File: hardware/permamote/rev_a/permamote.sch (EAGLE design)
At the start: 130 parts, among them J1 TC2030-JLINK-NL, J5 MICRO_USB_B_HIROSE_ZX62R-B-5P, Q1 PMDXB950UPEL, Q10 PMDXB950UPEL, Q2 PMDXB950UPEL, Q3 PMDXB950UPEL, Q4 PMDXB950UPEL, Q5 PMDXB950UPEL, Q6 PMDXB950UPEL, Q7 PMDXB950UPEL, Q8 PMDXB950UPEL, U1 AB1815-T3, U10 NRF52840, U11 SI7021-A20-GM1, U12 FT232RQ, U2 BQ25505, U3 EKMB1101111, U4 ISL29125, U5 LIS2DW12, U6 MAX17222, U7 MAX44009, U8 MS5637-02BA03, X1 32MHz, X3 32.768kHz, X4 ABS07-32.768KHZ-7-T

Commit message: Rename passives
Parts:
- removed C35: 4.7uF, passives:CAPACITOR0402_CAP
- removed C37, C38, C39: 10uF, passives:CAPACITOR0603_CAP
- removed C41: 0.1uF, passives:CAPACITOR0402_CAP
- removed C42, C43: DNP, passives:CAPACITOR0402_CAP
- removed L8: 1uH, passives:INDUCTORIHL
- removed R28: 6.19M, passives:RESISTOR0402_RES
- removed R29: 6.81M, passives:RESISTOR0402_RES
- removed U12: FT232RQ, ftdichip:FT232RQ
- added C14, C15, C16, C19: 0.1uF, passives:CAPACITOR0402_CAP
- added C28: 4.7uF, passives:CAPACITOR0603_CAP
- added C6: 12pF, passives:CAPACITOR0402_CAP
- added C9: 10nF, passives:CAPACITOR0402_CAP
- added L2: 15nH, passives:INDUCTOR0402
- added R19: 7.32M, passives:RESISTOR0402_RES
- added R20: 8.87M, passives:RESISTOR0402_RES
- added U9: MS5637-02BA03, chips:MS5637-02BA03
- C10: value 12pF -> 10nF; DIGIKEY 490-6197-1-ND -> 490-4516-1-ND
- C11: value 12pF -> 47nF; DIGIKEY 490-6197-1-ND -> 445-1264-1-ND
- C12: value 47pF -> 0.1uF; DIGIKEY 490-5942-1-ND -> 490-6328-1-ND
- C13: value 100pF -> 0.1uF; DIGIKEY 490-5922-1-ND -> 490-6328-1-ND
- C17: value 10nF -> 0.1uF; DIGIKEY 490-4516-1-ND -> 490-6328-1-ND
- C18: value 47nF -> 0.1uF; DIGIKEY 445-1264-1-ND -> 490-6328-1-ND
- C21, C22, C23, C24, C25: value 0.1uF -> 1uF; DIGIKEY 490-6328-1-ND -> 490-7195-1-ND
- C26, C27: value 0.1uF -> 4.7uF; DIGIKEY 490-6328-1-ND -> 445-5947-1-ND
- C29, C30, C31: value 1uF -> 10uF; device passives:CAPACITOR0402_CAP -> passives:CAPACITOR0603_CAP; DIGIKEY 490-7195-1-ND -> 490-3896-1-ND
- C3: value 0.01uF -> 12pF; DIGIKEY 490-4516-1-ND -> 490-6197-1-ND
- C32, C33: value 1uF -> DNP; DIGIKEY 490-7195-1-ND -> (none)
- C7: value 4.7uF -> 47pF; DIGIKEY 445-5947-1-ND -> 490-5942-1-ND
- C8: value 4.7uF -> 100pF; device passives:CAPACITOR0603_CAP -> passives:CAPACITOR0402_CAP; DIGIKEY 445-5947-1-ND -> 490-5922-1-ND
- L3: value 15nH -> 1uH; device passives:INDUCTOR0402 -> passives:INDUCTORIHL; DIGIKEY 587-1521-1-ND -> 541-1319-1-ND; MPN (none) -> IHLP1212BZER1R0M11
- R1, R2, R3: value 10kΩ -> 470; DIGIKEY 311-10KJRCT-ND -> 311-470JRCT-ND
- R10: value 6.04k -> 10k; DIGIKEY YAG3306CT-ND -> 311-10KJRCT-ND
- R11: value 3.9M -> 10k; DIGIKEY YAG3306CT-ND -> 311-10KJRCT-ND
- R12: value 8.87M -> 10k; DIGIKEY YAG3306CT-ND -> 311-10KJRCT-ND
- R13: value 4.22M -> 80.6k; device passives:RESISTOR0402_RES -> passives:RESISTOR0603_RES; DIGIKEY YAG3306CT-ND -> 311-80.6KHRCT-ND
- R14: value 7.32M -> 3.9M
- R15: value 9.09M -> 4.22M
- R17: value 470 -> 6.19M; DIGIKEY 311-470JRCT-ND -> YAG3306CT-ND
- R18: value 470 -> 6.81M; DIGIKEY 311-470JRCT-ND -> YAG3306CT-ND
- R21: value 6.04k -> 9.09M
- R22: value 33MΩ -> 33M
- R23, R24, R25, R26, R27: value 100MΩ -> 100M
- R4, R5: value 10kΩ -> 6.04k; DIGIKEY 311-10KJRCT-ND -> YAG3306CT-ND
- R6, R7: value 10kΩ -> 10k
- R8: value 470 -> 10k; DIGIKEY 311-470JRCT-ND -> 311-10KJRCT-ND
- R9: value 80.6kΩ -> 10k; device passives:RESISTOR0603_RES -> passives:RESISTOR0402_RES; DIGIKEY 311-80.6KHRCT-ND -> 311-10KJRCT-ND
- U4: value ISL29125 -> FT232RQ; device chips:ISL29125 -> ftdichip:FT232RQ
- U5: value LIS2DW12 -> ISL29125; device chips:LIS2DW12 -> chips:ISL29125
- U6: value MAX17222 -> LIS2DW12; device chips:MAX17222 -> chips:LIS2DW12
- U7: value MAX44009 -> MAX17222; device chips:MAX44009 -> chips:MAX17222
- U8: value MS5637-02BA03 -> MAX44009; device chips:MS5637-02BA03 -> chips:MAX44009
- renumbered L6 to L4, L7 to L5
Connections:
- net !CLR_INT: now also R8.1, U5.!INT; no longer R4.1, U4.!INT
- net !FTDI_RESET: now also U4.!RESET; no longer U12.!RESET
- net !LT_INT: now also R9.1, U8.!INT; no longer R5.1, U7.!INT
- net !RST: now also R11.1; no longer R7.1
- net !RTC_EXTR: now also R10.1; no longer R6.1
- net ACC_CS: now also U6.CS; no longer U5.CS
- net ACC_INT1: now also U6.INT1; no longer U5.INT1
- net ACC_INT2: now also U6.INT2; no longer U5.INT2
- net D+: now also U4.USBDP; no longer U12.USBDP
- net D-: now also U4.USBDM; no longer U12.USBDM
- net FTDI_VCCIO: now also U4.VCCIO; no longer U12.VCCIO
- net GND: now also C10.2, C11.2, C14.2, C15.2, C16.2, C19.2, C28.2, C3.1, C6.1, C9.2, R18.1, R21.1, U4.GND@1, U4.GND@2, U4.GND@A, U4.TEST, U8.A0, U9.GND; no longer C10.1, C11.1, C3.2, C35.2, C37.2, C38.2, C39.2, C41.2, C42.2, C43.2, R29.1, R9.1, U12.GND, U12.GND@1, U12.GND@2, U12.GND@A, U12.TEST, U7.A0
- net LED_BLUE: now also R3.2; no longer R18.2
- net LED_GREEN: now also R2.2; no longer R17.2
- net LED_RED: now also R1.2; no longer R8.2
- net MISO: now also U6.MISO/SA0; no longer U5.MISO/SA0
- net MOSI: now also U6.MOSI/SDA; no longer U5.MOSI/SDA
- net N$1: now also R14.2, R4.2; no longer R11.2, R21.2
- net N$12: now also R13.2, U7.SEL; no longer R9.2, U6.SEL
- net N$13: now also C20.1, U4.3V3OUT; no longer C41.1, U12.3V3OUT
- net N$14: now also U7.EN; no longer U6.EN
- net N$15: now also R1.1; no longer R8.1
- net N$16: now also R19.2, R5.2; no longer R10.2, R14.2
- net N$17: now also R2.1; no longer R17.1
- net N$18: now also R19.1, R21.2; no longer R11.1, R15.2
- net N$19: now also R3.1; no longer R18.1
- net N$2: now also C14.1; no longer C22.1
- net N$20: now also U8.VCC; no longer U7.VCC
- net N$21: now also U9.VDD; no longer U8.VDD
- net N$25: now also C7.1; no longer C12.1
- net N$26: now also C32.1; no longer C42.1
- net N$27: now also C33.1; no longer C43.1
- net N$3: now also C11.1, C22.1, L2.1; no longer C18.1, C30.1, L3.1
- net N$31: now also U5.VDD; no longer U4.VDD
- net N$34: now also U9.SCL; no longer U8.SCL
- net N$4: now also C8.1; no longer C13.1
- net N$41: now also U9.SDA; no longer U8.SDA
- net N$49: now also L2.2; no longer L3.2
- net N$51: now also U8.SDA; no longer U7.SDA
- net N$52: now also U8.SCL; no longer U7.SCL
- net N$54: now also U5.SDA; no longer U4.SDA
- net N$55: now also U5.SCL; no longer U4.SCL
- net N$57: now also R15.2, R17.1, R18.2, R20.1; no longer R12.1, R13.2, R28.1, R29.2
- net N$58: now also R17.2, R20.2, R4.1, R5.1; no longer R10.1, R12.2, R21.1, R28.2
- net N$8: now also C3.2; no longer C4.2
- net N$9: now also C4.2; no longer C5.2
- net RXD: now also U4.RXD; no longer U12.RXD
- net SCK: now also U6.SCL/SPC; no longer U5.SCL/SPC
- net SCL: now also R6.1; no longer R2.1
- net SDA: now also R7.1; no longer R3.1
- net SW: now also L3.2, U7.LX; no longer L8.2, U6.LX
- net TXD: now also U4.TXD; no longer U12.TXD
- net USB_5V: now also U4.VCC; no longer U12.VCC
- net VCC: now also C12.1, C13.1, C15.1, C16.1, C17.1, C18.1, C19.1, C30.1, R10.2, R11.2, R12.2, R8.2, R9.2, U6.VCC, U6.VDD_IO, U7.OUT; no longer C20.1, C27.1, C29.1, C32.1, C33.1, C35.1, C38.1, C39.1, R1.2, R2.2, R3.2, R4.2, R5.2, U5.VCC, U5.VDD_IO, U6.OUT
- net VOC_SAMP_VSTOR: now also C10.1, C27.1; no longer C3.1, C7.1
- net VREF_SAMP: now also C9.1; no longer C17.1
- net VSOL: now also C28.1; no longer C8.1
- net VSW: now also C29.1, L3.1, U7.IN; no longer C37.1, L8.1, U6.IN
- net WDI: now also R12.1; no longer R1.1
- net XL1: now also C6.2; no longer C11.2
- net XL2: now also C5.2; no longer C10.2
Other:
- moved on the sheet: C11, C12, C13, C21, C22, C24, C31, C33, C4, C5, R13, R14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

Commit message: update parts
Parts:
- C28: device passives:CAPACITOR0603_CAP -> passives:CAPACITOR0402_CAP
- J5: value MICRO_USB_B_HIROSE_ZX62R-B-5P -> MICRO_USB_B_HIROSE_ZX62R-B-5P(30); device connector:MICRO_USB_B_HIROSE_ZX62R-B-5P -> connector:MICRO_USB_B_HIROSE_ZX62R-B-5P(30)
- R14: DIGIKEY YAG3306CT-ND -> YAG3301CT-ND; MPN (none) -> RC0402JR-073M9L
- R15: value 4.22M -> DNP
- R16: value 5.62M -> DNP
- R17: value 6.19M -> 6.2M; DIGIKEY YAG3306CT-ND -> YAG3309CT-ND; MPN (none) -> RC0402JR-076M2L
- R18: value 6.81M -> 6.8M; DIGIKEY YAG3306CT-ND -> YAG3310CT-ND; MPN (none) -> RC0402JR-076M8L
- R19: value 7.32M -> DNP
- R20: value 8.87M -> DNP
- R21: value 9.09M -> 9.1M; DIGIKEY YAG3306CT-ND -> YAG3322CT-ND; MPN (none) -> RC0402JR-079M1L
- R4: DIGIKEY YAG3306CT-ND -> YAG2293CT-ND; MPN (none) -> RC0402FR-076K04L
- R5: value 6.04k -> DNP
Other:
- note added: "Divider for Other"
- note removed: "Divider for Lithium Polymer"
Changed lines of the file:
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@@
 <part name="Q6" library="fets" deviceset="PMDXB950UPEL" device=""/>
 <part name="R14" library="passives" deviceset="RESISTOR" device="0402_RES" value="3.9M">
-<attribute name="DIGIKEY" value="YAG3306CT-ND"/>
-</part>
-<part name="R21" library="passives" deviceset="RESISTOR" device="0402_RES" value="9.09M">
-<attribute name="DIGIKEY" value="YAG3306CT-ND"/>
+<attribute name="DIGIKEY" value="YAG3301CT-ND"/>
+<attribute name="MPN" value="RC0402JR-073M9L"/>
+</part>
+<part name="R21" library="passives" deviceset="RESISTOR" device="0402_RES" value="9.1M">
+<attribute name="DIGIKEY" value="YAG3322CT-ND"/>
+<attribute name="MPN" value="RC0402JR-079M1L"/>
 </part>
 <part name="GND21" library="supply1" library_urn="urn:adsk.eagle:library:371" deviceset="GND" device=""/>
 <part name="R4" library="passives" deviceset="RESISTOR" device="0402_RES" value="6.04k">
-<attribute name="DIGIKEY" value="YAG3306CT-ND"/>
-</part>
-<part name="R17" library="passives" deviceset="RESISTOR" device="0402_RES" value="6.19M">
-<attribute name="DIGIKEY" value="YAG3306CT-ND"/>
-</part>
-<part name="R18" library="passives" deviceset="RESISTOR" device="0402_RES" value="6.81M">
-<attribute name="DIGIKEY" value="YAG3306CT-ND"/>
+<attribute name="DIGIKEY" value="YAG2293CT-ND"/>
+<attribute name="MPN" value="RC0402FR-076K04L"/>
+</part>
+<part name="R17" library="passives" deviceset="RESISTOR" device="0402_RES" value="6.2M">
+<attribute name="DIGIKEY" value="YAG3309CT-ND"/>
+<attribute name="MPN" value="RC0402JR-076M2L"/>
+</part>
+<part name="R18" library="passives" deviceset="RESISTOR" device="0402_RES" value="6.8M">
+<attribute name="DIGIKEY" value="YAG3310CT-ND"/>
+<attribute name="MPN" value="RC0402JR-076M8L"/>
 </part>
 <part name="GND22" library="supply1" library_urn="urn:adsk.eagle:library:371" deviceset="GND" device=""/>
@@
 <part name="GND19" library="supply1" library_urn="urn:adsk.eagle:library:371" deviceset="GND" device=""/>
 <part name="SJ1" library="jumper" library_urn="urn:adsk.eagle:library:252" deviceset="SJ2W" device="" package3d_urn="urn:adsk.eagle:package:15474/1"/>
-<part name="R5" library="passives" deviceset="RESISTOR" device="0402_RES" value="6.04k">
+<part name="R5" library="passives" deviceset="RESISTOR" device="0402_RES" value="DNP">
 <attribute name="DIGIKEY" value="YAG3306CT-ND"/>
 </part>
-<part name="R20" library="passives" deviceset="RESISTOR" device="0402_RES" value="8.87M">
+<part name="R20" library="passives" deviceset="RESISTOR" device="0402_RES" value="DNP">
 <attribute name="DIGIKEY" value="YAG3306CT-ND"/>
 </part>
-<part name="R15" library="passives" deviceset="RESISTOR" device="0402_RES" value="4.22M">
+<part name="R15" library="passives" deviceset="RESISTOR" device="0402_RES" value="DNP">
 <attribute name="DIGIKEY" value="YAG3306CT-ND"/>
 </part>
 <part name="BT2" library="batteries" deviceset="BAT-HLD-002-THM" device=""/>
 <part name="BT3" library="batteries" deviceset="BAT-HLD-002-THM" device=""/>
-<part name="R19" library="passives" deviceset="RESISTOR" device="0402_RES" value="7.32M">
+<part name="R19" library="passives" deviceset="RESISTOR" device="0402_RES" value="DNP">
 <attribute name="DIGIKEY" value="YAG3306CT-ND"/>
 </part>
-<part name="R16" library="passives" deviceset="RESISTOR" device="0402_RES" value="5.62M">
+<part name="R16" library="passives" deviceset="RESISTOR" device="0402_RES" value="DNP">
 <attribute name="DIGIKEY" value="YAG3306CT-ND"/>
 </part>
@@
 <attribute name="DIGIKEY" value="311-10KJRCT-ND "/>
 </part>
-<part name="J5" library="connector" deviceset="MICRO_USB_B_HIROSE_ZX62R-B-5P" device=""/>
+<part name="J5" library="connector" deviceset="MICRO_USB_B_HIROSE_ZX62R-B-5P(30)" device=""/>
 <part name="P+16" library="supply1" library_urn="urn:adsk.eagle:library:371" deviceset="VCC" device=""/>
 <part name="P+18" library="supply1" library_urn="urn:adsk.eagle:library:371" deviceset="VCC" device=""/>
@@
 <attribute name="DIGIKEY" value="445-5947-1-ND"/>
 </part>
-<part name="C28" library="passives" deviceset="CAPACITOR" device="0603_CAP" value="4.7uF">
+<part name="C28" library="passives" deviceset="CAPACITOR" device="0402_CAP" value="4.7uF">
 <attribute name="DIGIKEY" value="445-5947-1-ND"/>
 </part>
@@
 <text x="2.54" y="66.04" size="2.54" layer="97">Boost Regulator</text>
 <text x="124.46" y="53.34" size="1.778" layer="98" rot="R90" align="bottom-center">Divider for Lithium Titanate</text>
-<text x="162.56" y="53.34" size="1.778" layer="98" rot="R90" align="bottom-center">Divider for Lithium Polymer</text>
+<text x="162.56" y="53.34" size="1.778" layer="98" rot="R90" align="bottom-center">Divider for Other</text>
 </plain>
 <instances>
@@
 <instance part="R14" gate="G$1" x="116.84" y="58.42" rot="R90">
 <attribute name="DIGIKEY" x="116.84" y="58.42" size="1.778" layer="96" rot="R90" display="off"/>
+<attribute name="MPN" x="116.84" y="58.42" size="1.778" layer="96" rot="R90" display="off"/>
 </instance>
 <instance part="R21" gate="G$1" x="116.84" y="45.72" rot="R90">
 <attribute name="DIGIKEY" x="116.84" y="45.72" size="1.778" layer="96" rot="R90" display="off"/>
+<attribute name="MPN" x="116.84" y="45.72" size="1.778" layer="96" rot="R90" display="off"/>
 </instance>
 <instance part="GND21" gate="1" x="116.84" y="27.94"/>
 <instance part="R4" gate="G$1" x="137.16" y="71.12" rot="R90">
 <attribute name="DIGIKEY" x="137.16" y="71.12" size="1.778" layer="96" rot="R90" display="off"/>
+<attribute name="MPN" x="137.16" y="71.12" size="1.778" layer="96" rot="R90" display="off"/>
 </instance>
 <instance part="R17" gate="G$1" x="137.16" y="58.42" rot="R90">
 <attribute name="DIGIKEY" x="137.16" y="58.42" size="1.778" layer="96" rot="R90" display="off"/>
+<attribute name="MPN" x="137.16" y="58.42" size="1.778" layer="96" rot="R90" display="off"/>
 </instance>
 <instance part="R18" gate="G$1" x="137.16" y="45.72" rot="R90">
 <attribute name="DIGIKEY" x="137.16" y="45.72" size="1.778" layer="96" rot="R90" display="off"/>
+<attribute name="MPN" x="137.16" y="45.72" size="1.778" layer="96" rot="R90" display="off"/>
 </instance>
 <instance part="GND22" gate="1" x="137.16" y="27.94"/>

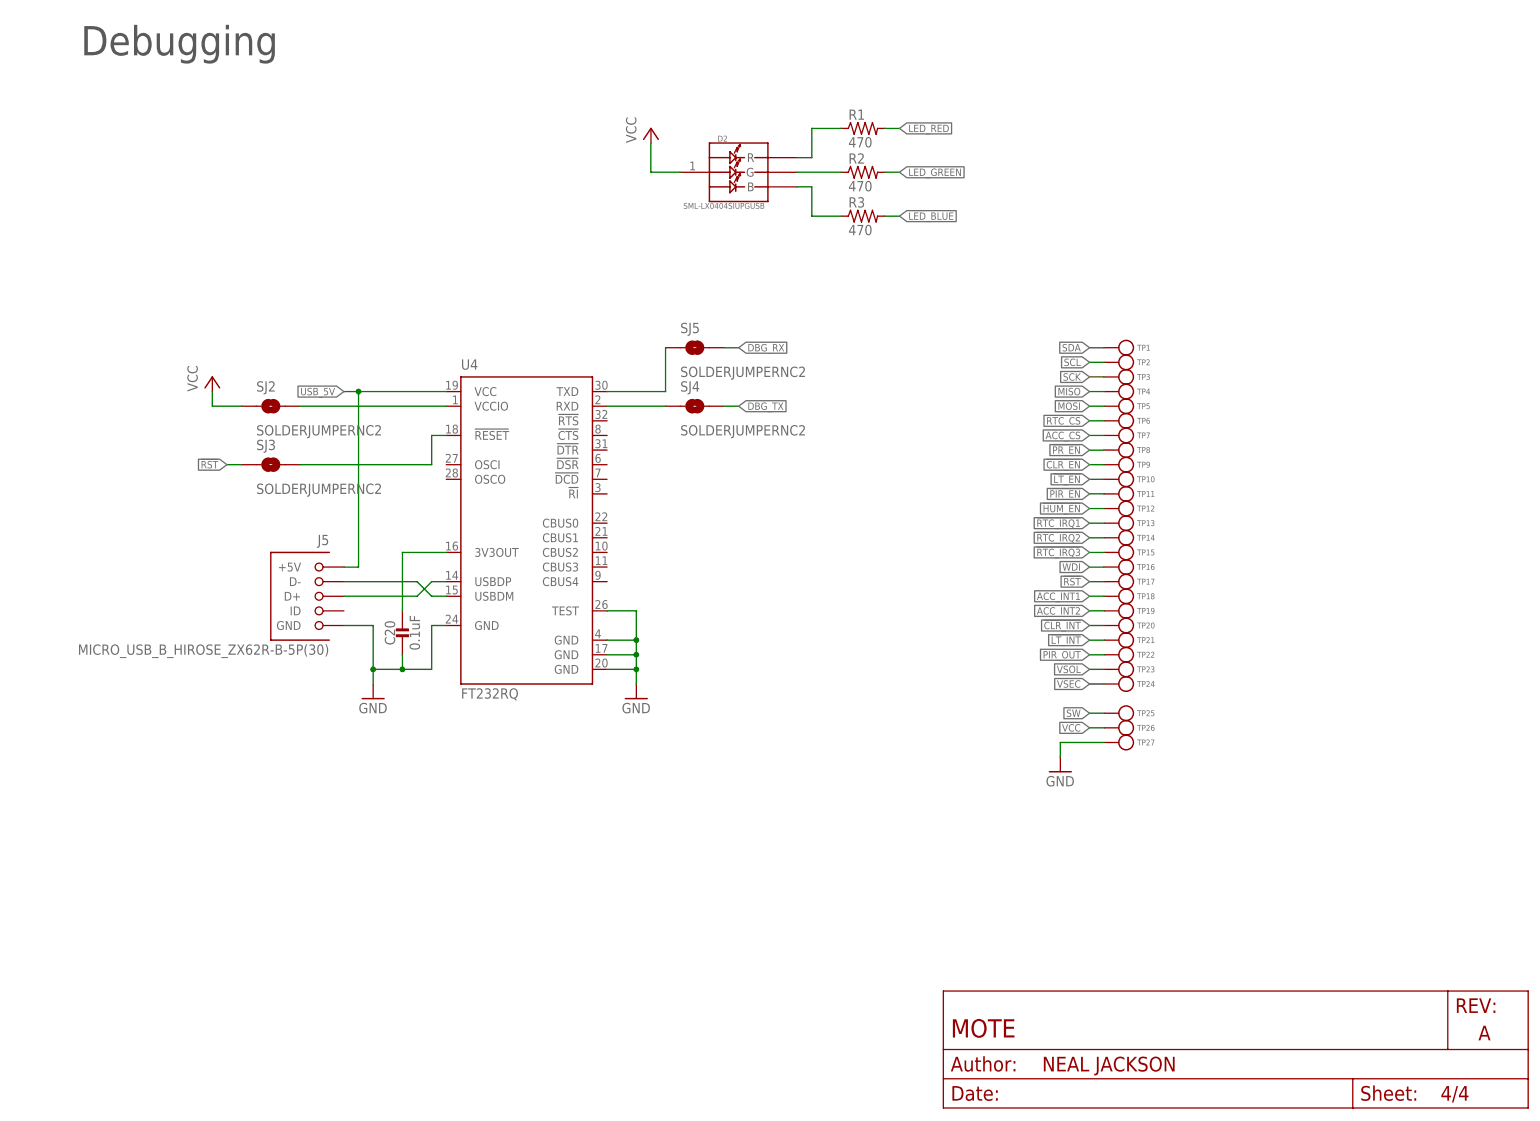
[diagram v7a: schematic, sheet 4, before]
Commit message: clean up schematic
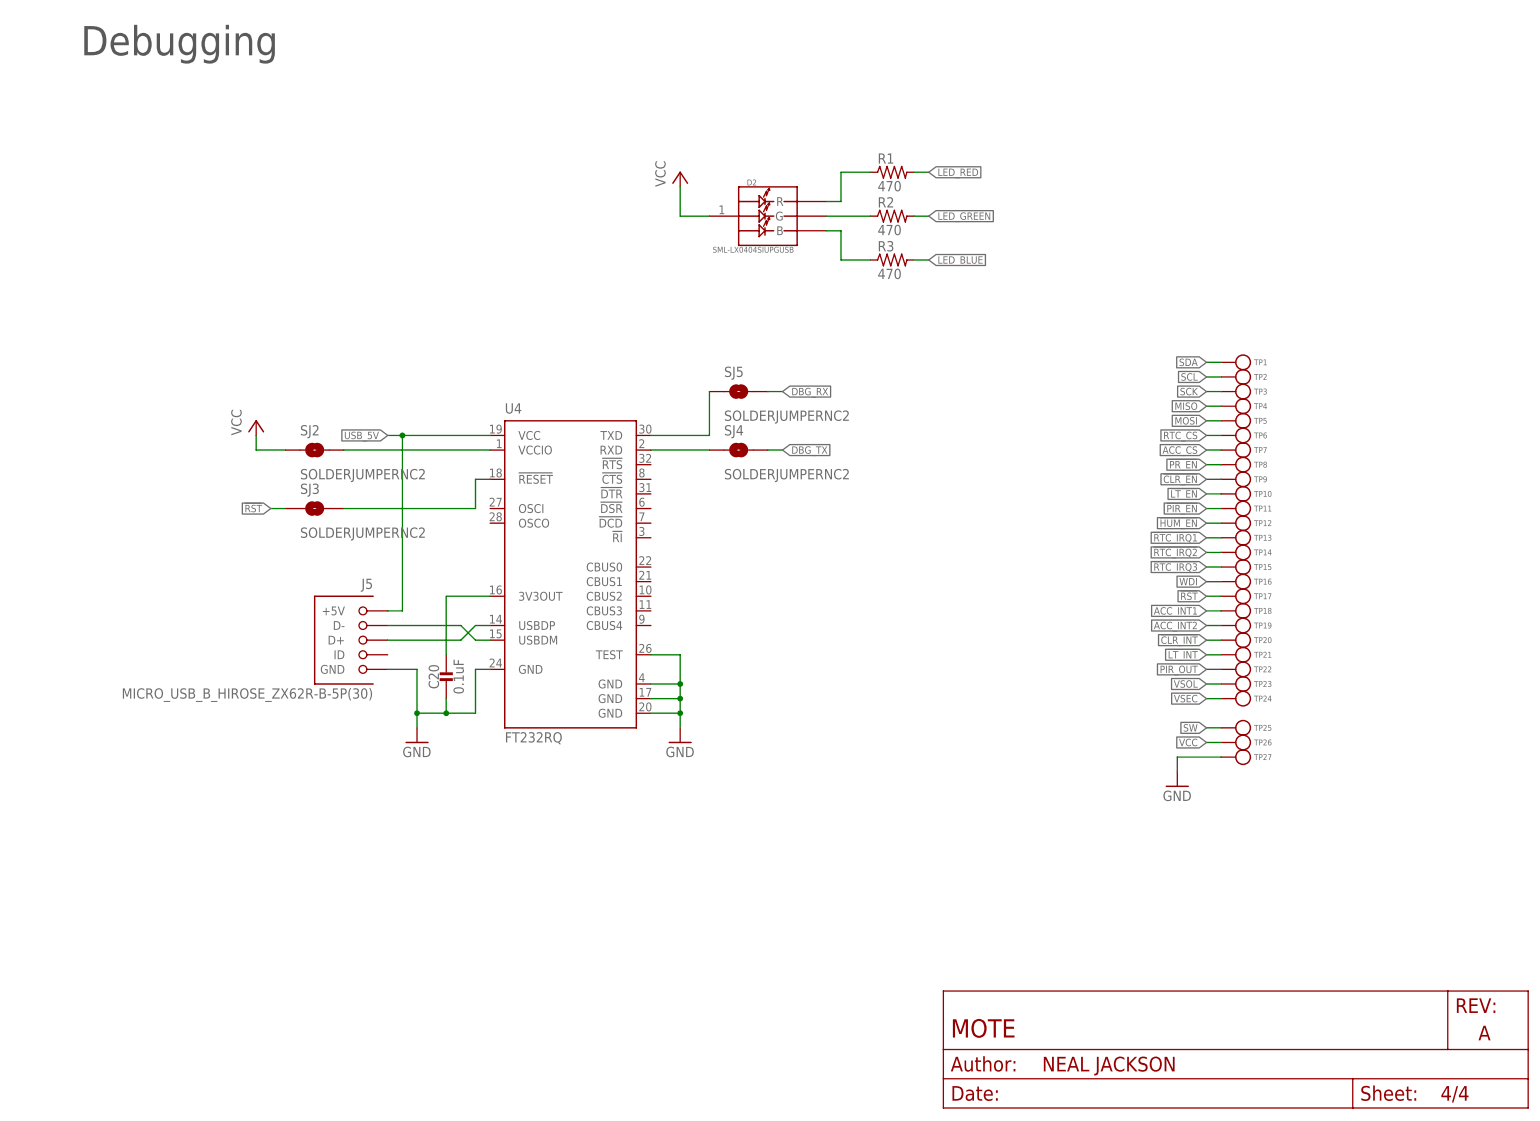
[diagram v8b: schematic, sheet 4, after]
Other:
- note added: "Do Not Populate I2C pull-up (NRF has internal pull-up)"
- moved on the sheet: C20, D2, J5, R1, R2, R3, SJ2, SJ3, SJ4, SJ5, TP1, TP10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
